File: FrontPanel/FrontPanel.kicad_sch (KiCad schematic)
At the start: 72 parts, among them SW1 Channel 1, SW10 5, SW11 2, SW12 0, SW13 9, SW14 6, SW15 3, SW16 Backspace, SW17 Voltage 1, SW18 Current 1, SW19 Voltage 2, SW2 Confirm, SW20 Current 2, SW3 Cancel, SW4 Channel 2, SW5 7, SW6 4, SW7 1, SW8 Decimal, SW9 8

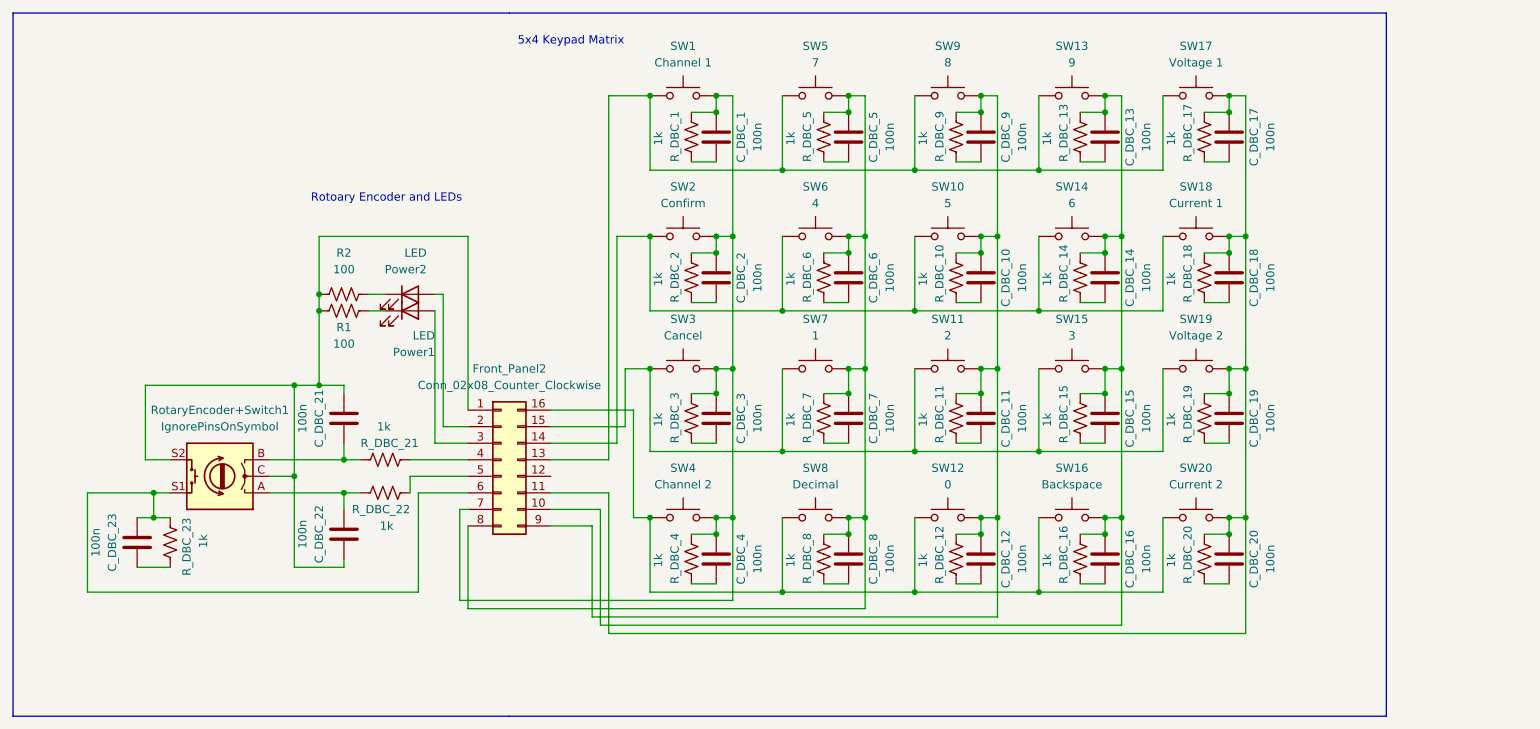
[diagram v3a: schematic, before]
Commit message: Fix front panel and routed main regulator
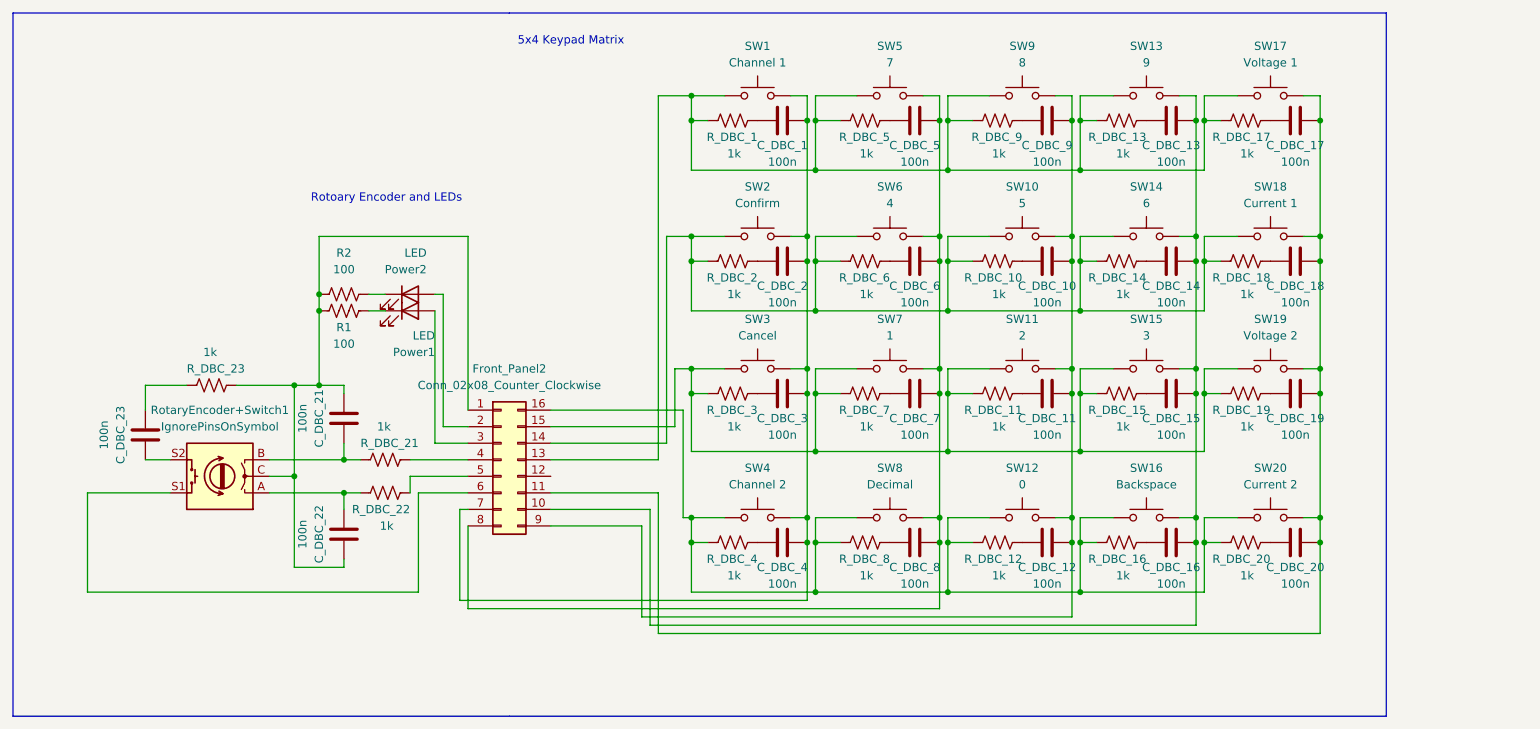
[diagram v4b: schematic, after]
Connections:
- net at C_DBC_17.2, C_DBC_18.2, C_DBC_19.2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: no longer R_DBC_17.1, R_DBC_18.1, R_DBC_19.1, R_DBC_20.1
- net at Front_Panel2.14 (Pin_14), SW10.1, SW14.1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: now also R_DBC_10.1, R_DBC_14.1, R_DBC_18.1, R_DBC_2.1, R_DBC_6.1
- net at C_DBC_13.2, C_DBC_14.2, C_DBC_15.2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: no longer R_DBC_13.1, R_DBC_14.1, R_DBC_15.1, R_DBC_16.1
- net at R_DBC_23.1: now also C_DBC_21.1, C_DBC_22.2, Front_Panel2.1 (Pin_1), R1.2, R2.2, RotaryEncoder+Switch1.C; no longer C_DBC_23.2
- net at C_DBC_23.1, R_DBC_23.2: no longer Front_Panel2.6 (Pin_6), RotaryEncoder+Switch1.S1
- net at Front_Panel2.16 (Pin_16), SW12.1, SW16.1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: now also R_DBC_12.1, R_DBC_16.1, R_DBC_20.1, R_DBC_4.1, R_DBC_8.1
- net at C_DBC_10.2, C_DBC_11.2, C_DBC_12.2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: no longer R_DBC_10.1, R_DBC_11.1, R_DBC_12.1, R_DBC_9.1
- net at Front_Panel2.15 (Pin_15), SW11.1, SW15.1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: now also R_DBC_11.1, R_DBC_15.1, R_DBC_19.1, R_DBC_3.1, R_DBC_7.1
- net at C_DBC_5.2, C_DBC_6.2, C_DBC_7.2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: no longer R_DBC_5.1, R_DBC_6.1, R_DBC_7.1, R_DBC_8.1
- net at C_DBC_1.2, C_DBC_2.2, C_DBC_3.2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: no longer R_DBC_1.1, R_DBC_2.1, R_DBC_3.1, R_DBC_4.1
- net at Front_Panel2.13 (Pin_13), SW1.1, SW13.1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: now also R_DBC_1.1, R_DBC_13.1, R_DBC_17.1, R_DBC_5.1, R_DBC_9.1
- new net: C_DBC_23.2, RotaryEncoder+Switch1.S2
- new net: Front_Panel2.6 (Pin_6), RotaryEncoder+Switch1.S1
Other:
- moved on the sheet: C_DBC_1, C_DBC_10, C_DBC_11, C_DBC_12, C_DBC_13, C_DBC_14, C_DBC_15, C_DBC_16, C_DBC_17, C_DBC_18, C_DBC_19, C_DBC_2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

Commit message: Rerouted front panel with less vias
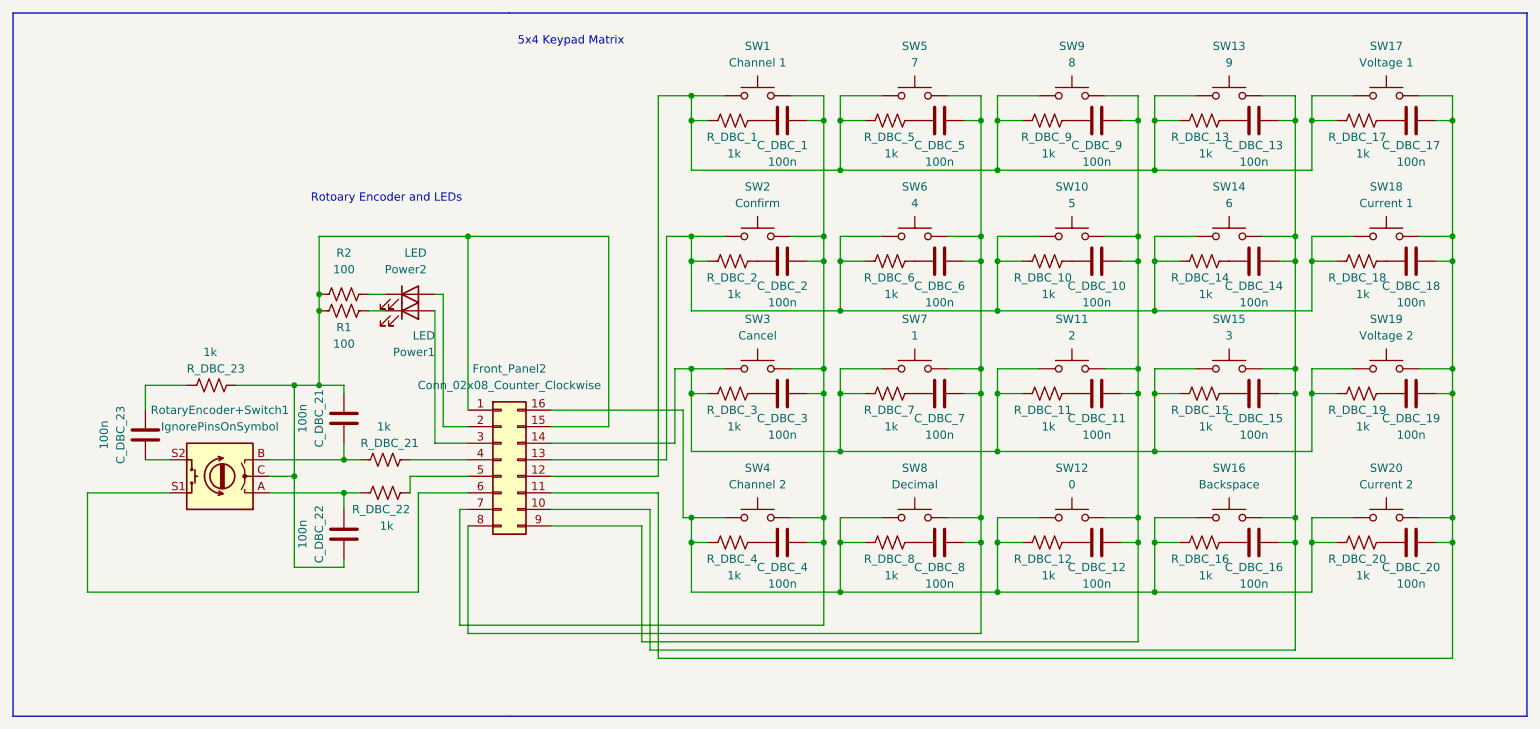
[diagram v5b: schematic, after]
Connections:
- net at R_DBC_10.1, R_DBC_14.1, R_DBC_18.1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: now also Front_Panel2.13 (Pin_13); no longer Front_Panel2.14 (Pin_14)
- net at C_DBC_21.1, C_DBC_22.2, Front_Panel2.1 (Pin_1)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: now also Front_Panel2.15 (Pin_15)
- net at R_DBC_11.1, R_DBC_15.1, R_DBC_19.1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: now also Front_Panel2.14 (Pin_14); no longer Front_Panel2.15 (Pin_15)
- net at R_DBC_1.1, R_DBC_13.1, R_DBC_17.1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: now also Front_Panel2.12 (Pin_12); no longer Front_Panel2.13 (Pin_13)
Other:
- moved on the sheet: C_DBC_10, C_DBC_11, C_DBC_12, C_DBC_13, C_DBC_14, C_DBC_15, C_DBC_16, C_DBC_17, C_DBC_18, C_DBC_19, C_DBC_20, C_DBC_5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
